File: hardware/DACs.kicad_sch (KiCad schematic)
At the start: 70 parts, among them U10 LTC2642ACDD-16#PBF, U11 LTC2642ACDD-16#PBF, U12 LTC2642ACDD-16#PBF, U13 LT1678CS8#PBF, U14 LT1678CS8#PBF, U15 LT1678CS8#PBF, U16 LT1678CS8#PBF, U17 LT1461CIS8-2.5#PBF, U9 LTC2642ACDD-16#PBF

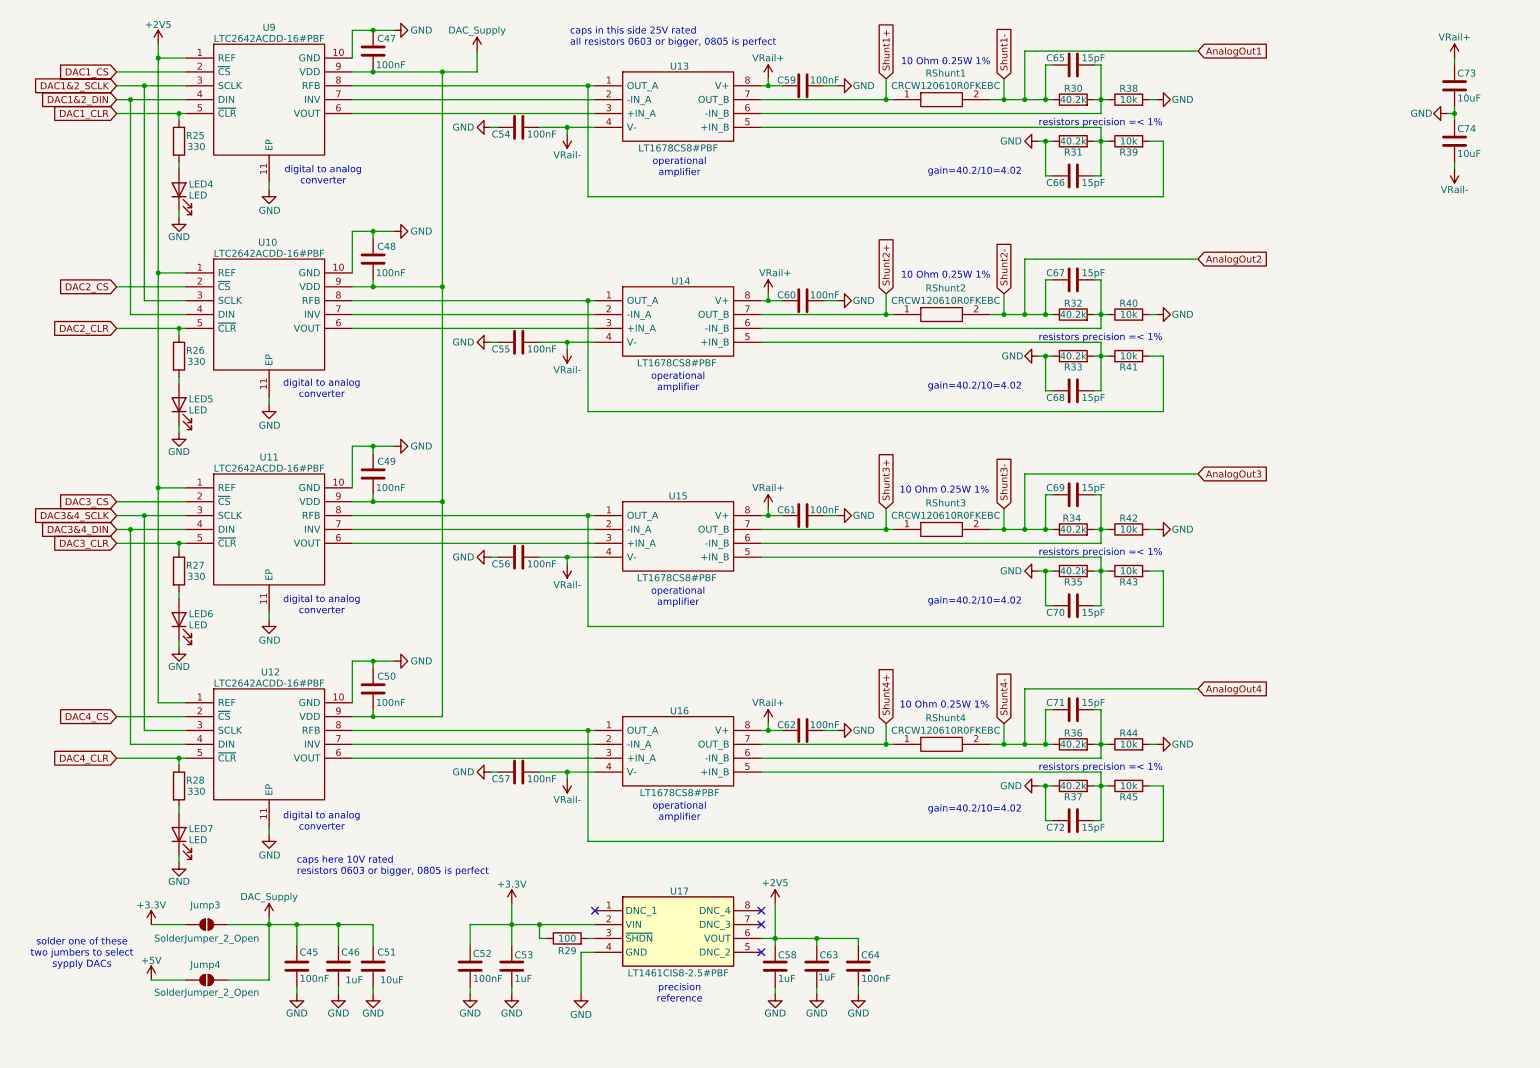
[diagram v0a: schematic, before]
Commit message: Added caps voltage rating + block diagram
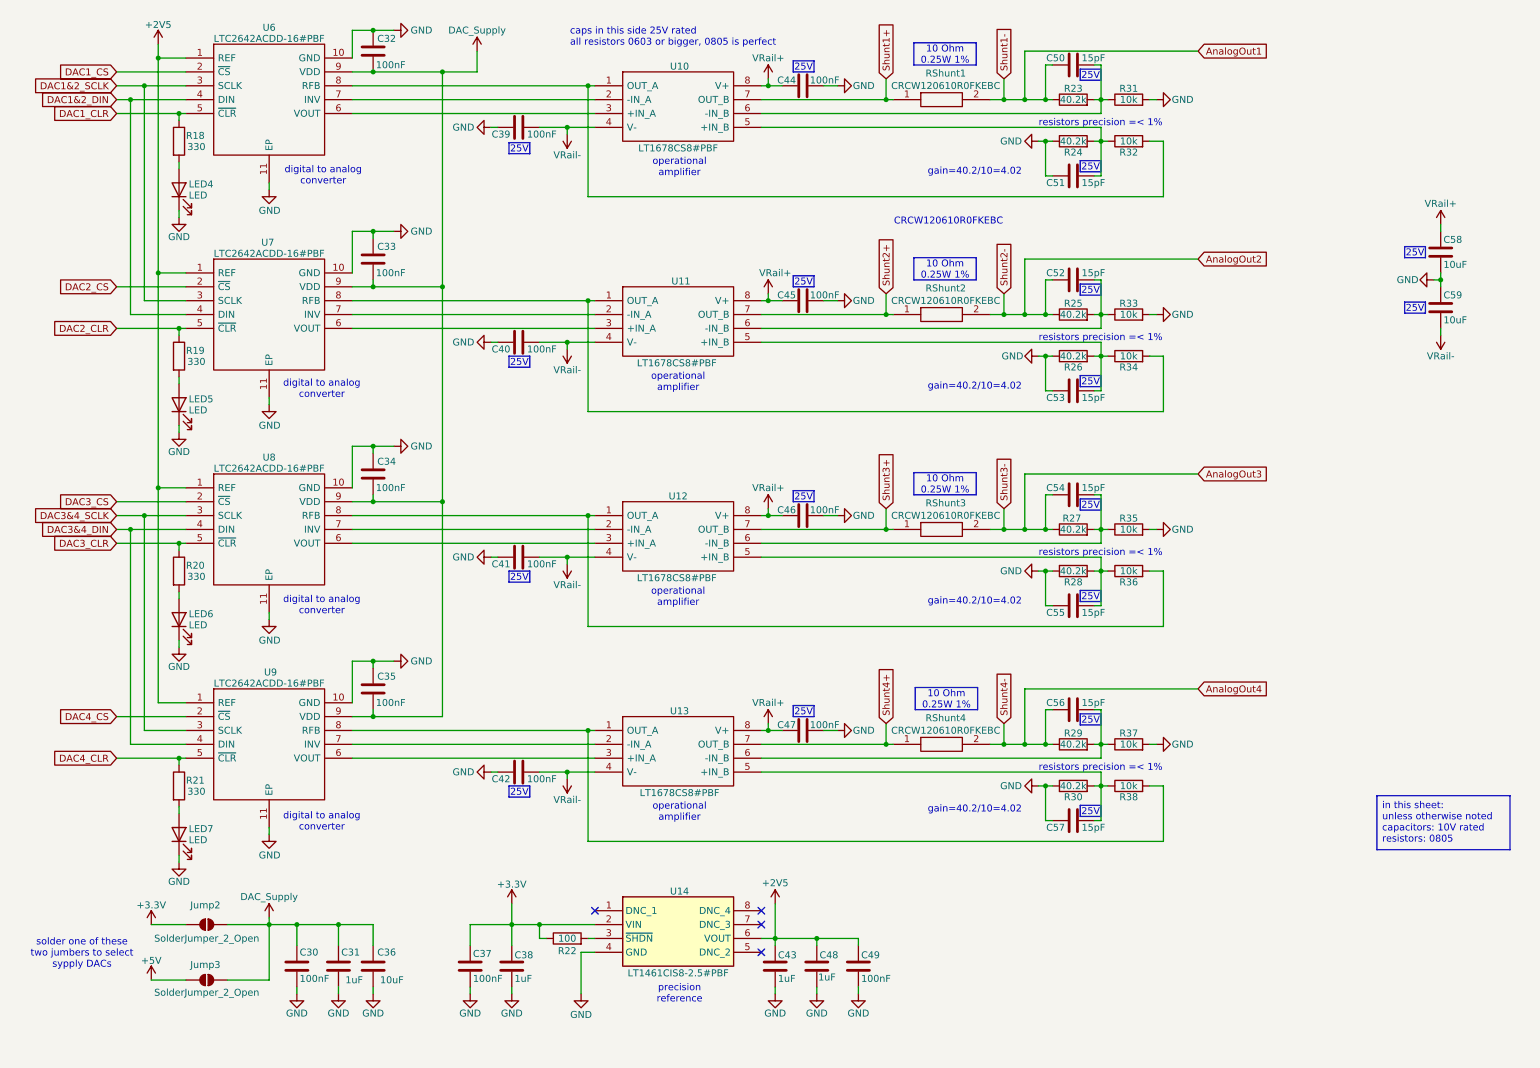
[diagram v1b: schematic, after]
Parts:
- renumbered C45 to C30, C46 to C31, C47 to C32, C48 to C33, C49 to C34, C50 to C35, C51 to C36, C52 to C37, C53 to C38, C54 to C39, C55 to C40, C56 to C41, C57 to C42, C58 to C43, C59 to C44, C60 to C45, C61 to C46, C62 to C47, C63 to C48, C64 to C49, C65 to C50, C66 to C51, C67 to C52, C68 to C53, C69 to C54, C70 to C55, C71 to C56, C72 to C57, C73 to C58, C74 to C59, Jump3 to Jump2, Jump4 to Jump3, R25 to R18, R26 to R19, R27 to R20, R28 to R21, R29 to R22, R30 to R23, R31 to R24, R32 to R25, R33 to R26, R34 to R27, R35 to R28, R36 to R29, R37 to R30, R38 to R31, R39 to R32, R40 to R33, R41 to R34, R42 to R35, R43 to R36, R44 to R37, R45 to R38, U13 to U10, U14 to U11, U15 to U12, U16 to U13, U17 to U14, U9 to U6, U10 to U7, U11 to U8, U12 to U9
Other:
- note added: "CRCW120610R0FKEBC"
- note removed: "10 Ohm 0.25W 1%"
- note removed: "caps here 10V rated resistors 0603 or bigger, 0805 is perfect"
- title: Multi Channel HARP DAC -> harp device quad dac
- moved on the sheet: C58, C59

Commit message: The footprint assigning and reviewing have started.
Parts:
- C30, C31, C32, C33, C34, C35, C36, C37, C38, C39, C40, C41, C42, C43, C44, C45, C46, C47, C48, C49, C50, C51, C52, C53, C54, C55, C56, C57, C58, C59: symbol Device:C -> harp.device.quad.dac:C
- Jump2, Jump3: symbol Jumper:SolderJumper_2_Open -> harp.device.quad.dac:SolderJumper_2_Open
- LED4, LED5, LED6, LED7: symbol Device:LED -> harp.device.quad.dac:LED
- R18, R19, R20, R21, R22, R23, R24, R25, R26, R27, R28, R29, R30, R31, R32, R33, R34, R35, R36, R37, R38: symbol Device:R -> harp.device.quad.dac:R
- RShunt1, RShunt2, RShunt3, RShunt4: symbol CRCW120610R0FKEBC:CRCW120610R0FKEBC -> harp.device.quad.dac:CRCW120610R0FKEBC
- U10, U11, U12, U13: symbol LT1678CS8#PBF:LT1678CS8#PBF -> harp.device.quad.dac:LT1678CS8#PBF
- U14: symbol LT1461CIS8-2_5#PBF:LT1461CIS8-2.5#PBF -> harp.device.quad.dac:LT1461CIS8-2.5#PBF
- U6, U7, U8, U9: symbol LTC2642ACDD-16#PBF:LTC2642ACDD-16#PBF -> harp.device.quad.dac:LTC2642ACDD-16#PBF

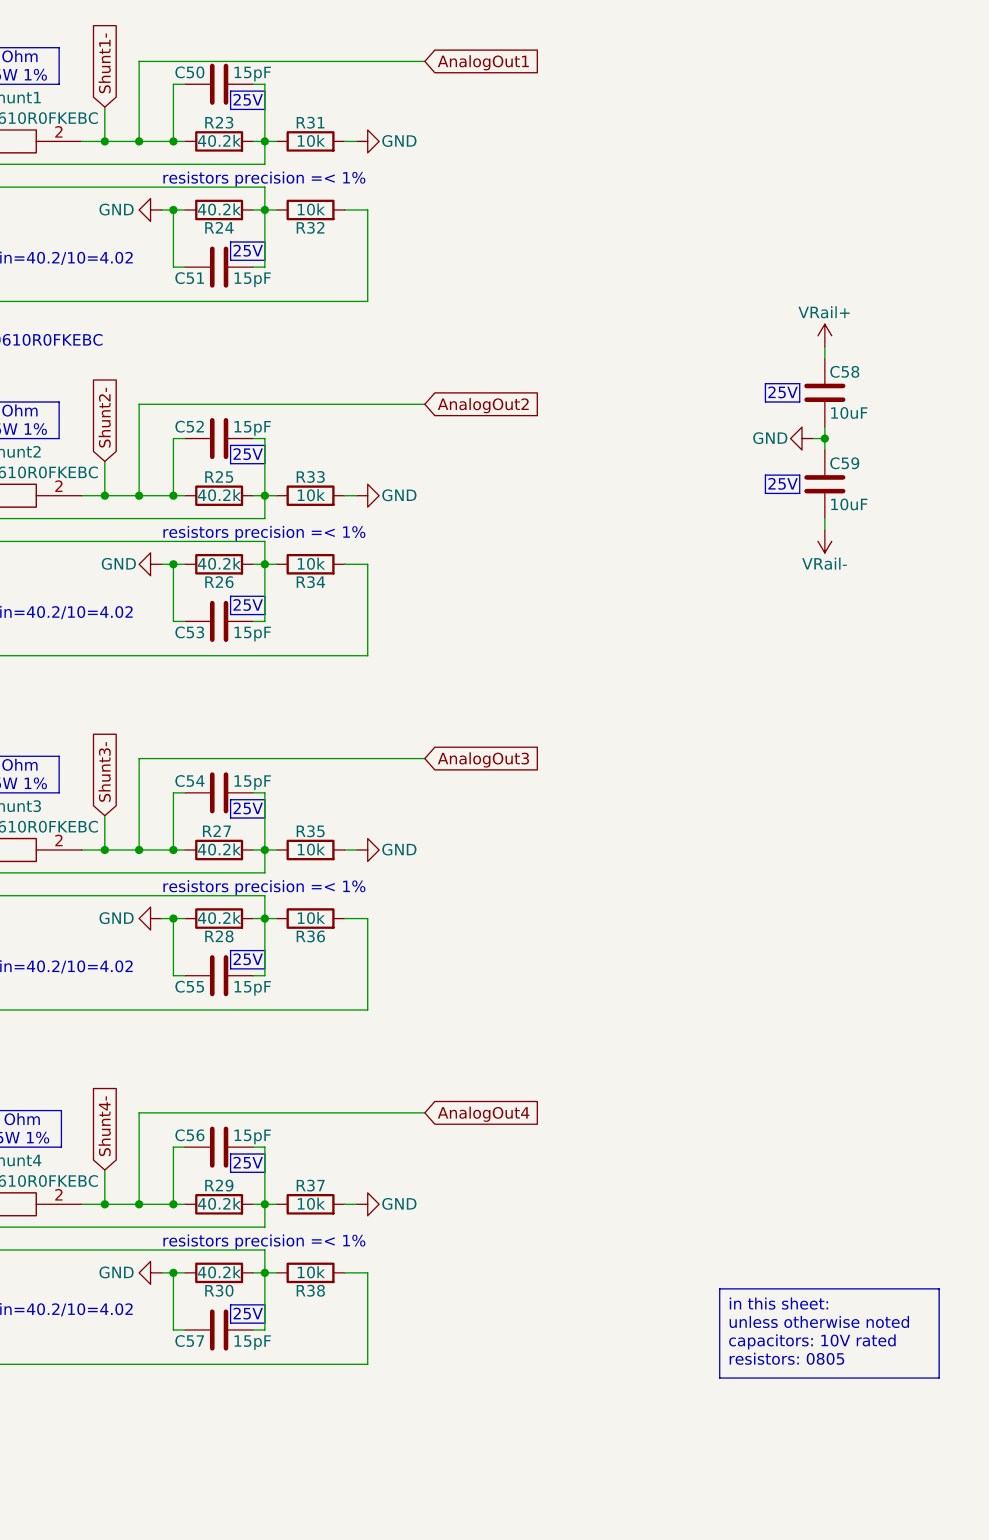
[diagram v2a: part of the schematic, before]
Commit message: Modified notes about caps and resistors
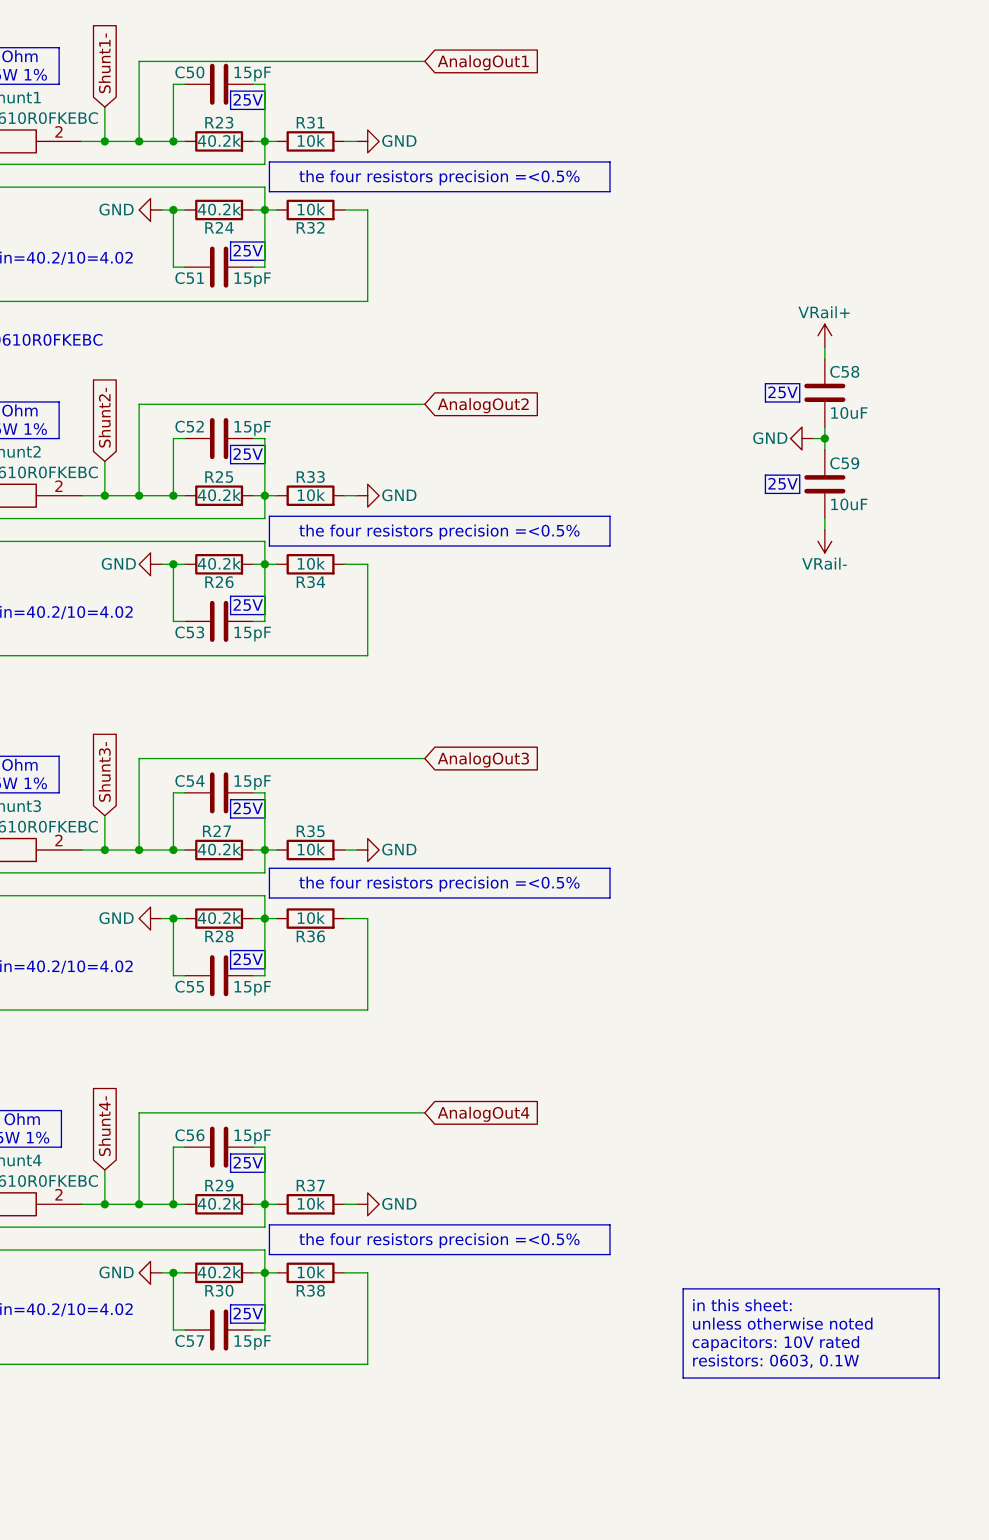
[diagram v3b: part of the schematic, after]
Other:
- note removed: "resistors precision =< 1%"
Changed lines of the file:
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@@
 		)
 	)
-	(text "resistors precision =< 1%"
-		(exclude_from_sim no)
-		(at 198.12 151.13 0)
+	(text "operational\namplifier"
+		(exclude_from_sim no)
+		(at 132.08 120.904 0)
+		(effects
+			(font
+				(size 1.27 1.27)
+			)
+			(justify bottom)
+		)
+	)
+	(text "gain=40.2/10=4.02"
+		(exclude_from_sim no)
+		(at 177.8 81.28 0)
 		(effects
 			(font
@@
 		)
 	)
+	(text "digital to analog\nconverter"
+		(exclude_from_sim no)
+		(at 66.802 162.052 0)
+		(effects
+			(font
+				(size 1.27 1.27)
+			)
+			(justify bottom)
+		)
+	)
+	(text "digital to analog\nconverter"
+		(exclude_from_sim no)
+		(at 66.802 122.428 0)
+		(effects
+			(font
+				(size 1.27 1.27)
+			)
+			(justify bottom)
+		)
+	)
+	(text "CRCW120610R0FKEBC"
+		(exclude_from_sim no)
+		(at 181.61 50.292 0)
+		(effects
+			(font
+				(size 1.27 1.27)
+			)
+		)
+	)
 	(text "operational\namplifier"
 		(exclude_from_sim no)
-		(at 132.08 120.904 0)
+		(at 132.334 160.274 0)
 		(effects
 			(font
@@
 		)
 	)
+	(text "caps in this side 25V rated\nall resistors 0603 or bigger, 0805 is perfect"
+		(exclude_from_sim no)
+		(at 112.268 16.51 0)
+		(effects
+			(font
+				(size 1.27 1.27)
+			)
+			(justify left)
+		)
+	)
 	(text "gain=40.2/10=4.02"
 		(exclude_from_sim no)
-		(at 177.8 81.28 0)
+		(at 177.8 158.75 0)
 		(effects
 			(font
@@
 	(text "digital to analog\nconverter"
 		(exclude_from_sim no)
-		(at 66.802 162.052 0)
+		(at 67.056 43.688 0)
 		(effects
 			(font
@@
 		)
 	)
-	(text "digital to analog\nconverter"
-		(exclude_from_sim no)
-		(at 66.802 122.428 0)
-		(effects
-			(font
-				(size 1.27 1.27)
-			)
-			(justify bottom)
-		)
-	)
-	(text "CRCW120610R0FKEBC"
-		(exclude_from_sim no)
-		(at 181.61 50.292 0)
-		(effects
-			(font
-				(size 1.27 1.27)
-			)
-		)
-	)
-	(text "resistors precision =< 1%"
-		(exclude_from_sim no)
-		(at 198.12 72.39 0)
+	(text "gain=40.2/10=4.02"
+		(exclude_from_sim no)
+		(at 177.8 120.65 0)
 		(effects
 			(font
@@
 		)
 	)
-	(text "operational\namplifier"
-		(exclude_from_sim no)
-		(at 132.334 160.274 0)
-		(effects
-			(font
-				(size 1.27 1.27)
-			)
-			(justify bottom)
-		)
-	)
-	(text "caps in this side 25V rated\nall resistors 0603 or bigger, 0805 is perfect"
-		(exclude_from_sim no)
-		(at 112.268 16.51 0)
-		(effects
-			(font
-				(size 1.27 1.27)
-			)
-			(justify left)
-		)
-	)
-	(text "gain=40.2/10=4.02"
-		(exclude_from_sim no)
-		(at 177.8 158.75 0)
-		(effects
-			(font
-				(size 1.27 1.27)
-			)
-			(justify left bottom)
-		)
-	)
-	(text "resistors precision =< 1%"
-		(exclude_from_sim no)
-		(at 198.12 33.02 0)
-		(effects
-			(font
-				(size 1.27 1.27)
-			)
-			(justify left bottom)
-		)
-	)
-	(text "digital to analog\nconverter"
-		(exclude_from_sim no)
-		(at 67.056 43.688 0)
-		(effects
-			(font
-				(size 1.27 1.27)
-			)
-			(justify bottom)
-		)
-	)
-	(text "gain=40.2/10=4.02"
-		(exclude_from_sim no)
-		(at 177.8 120.65 0)
-		(effects
-			(font
-				(size 1.27 1.27)
-			)
-			(justify left bottom)
-		)
-	)
 	(text "solder one of these\ntwo jumbers to select\nsypply DACs"
 		(exclude_from_sim no)
@@
 				(size 1.27 1.27)
 			)
-		)
-	)
-	(text "resistors precision =< 1%"
-		(exclude_from_sim no)
-		(at 198.12 111.76 0)
-		(effects
-			(font
-				(size 1.27 1.27)
-			)
-			(justify left bottom)
 		)
 	)
@@
 		)
 	)
-	(text_box "in this sheet:\nunless otherwise noted\ncapacitors: 10V rated \nresistors: 0805"
-		(exclude_from_sim no)
-		(at 260.096 155.448 0)
-		(size 24.384 9.906)
-		(margins 0.9525 0.9525 0.9525 0.9525)
-		(stroke
-			(width 0)
-			(type solid)
-		)
-		(fill
-			(type color)
-			(color 0 255 0 1)
-		)
-		(effects
-			(font
-				(size 1.27 1.27)
-			)
-			(justify left top)
+	(text_box "in this sheet:\nunless otherwise noted\ncapacitors: 10V rated \nresistors: 0603, 0.1W"
+		(exclude_from_sim no)
+		(at 256.032 155.448 0)
+		(size 28.448 9.906)
+		(margins 0.9525 0.9525 0.9525 0.9525)
+		(stroke
+			(width 0)
+			(type solid)
+		)
+		(fill
+			(type color)
+			(color 0 255 0 1)
+		)
+		(effects
+			(font
+				(size 1.27 1.27)
+			)
+			(justify left)
 		)
 	)
@@
 		)
 	)
+	(text_box "the four resistors precision =<0.5%"
+		(exclude_from_sim no)
+		(at 210.058 148.336 0)
+		(size 37.846 3.302)
+		(margins 0.9525 0.9525 0.9525 0.9525)
+		(stroke
+			(width 0)
+			(type solid)
+		)
+		(fill
+			(type color)
+			(color 0 255 0 1)
+		)
+		(effects
+			(font
+				(size 1.27 1.27)
+			)
+		)
+	)
 	(text_box "25V"
 		(exclude_from_sim no)
@@
 		)
 	)
+	(text_box "the four resistors precision =<0.5%"
+		(exclude_from_sim no)
+		(at 210.058 30.226 0)
+		(size 37.846 3.302)
+		(margins 0.9525 0.9525 0.9525 0.9525)
+		(stroke
+			(width 0)
+			(type solid)
+		)
+		(fill
+			(type color)
+			(color 0 255 0 1)
+		)
+		(effects
+			(font
+				(size 1.27 1.27)
+			)
+		)
+	)
 	(text_box "25V"
 		(exclude_from_sim no)
 		(at 101.092 35.814 0)
 		(size 3.81 2.032)
+		(margins 0.9525 0.9525 0.9525 0.9525)
+		(stroke
+			(width 0)
+			(type solid)
+		)
+		(fill
+			(type color)
+			(color 0 255 0 1)
+		)
+		(effects
+			(font
+				(size 1.27 1.27)
+			)
+		)
+	)
+	(text_box "the four resistors precision =<0.5%"
+		(exclude_from_sim no)
+		(at 210.058 108.712 0)
+		(size 37.846 3.302)
 		(margins 0.9525 0.9525 0.9525 0.9525)
 		(stroke
@@
 		(margins 0.9525 0.9525 0.9525 0.9525)
 		(stroke
+			(width 0)
+			(type solid)
+		)
+		(fill
+			(type color)
+			(color 0 255 0 1)
+		)
+		(effects
+			(font
+				(size 1.27 1.27)
+			)
+		)
+	)
+	(text_box "the four resistors precision =<0.5%"
+		(exclude_from_sim no)
+		(at 210.058 69.596 0)
+		(size 37.846 3.302)
+		(margins 0.9525 0.9525 0.9525 0.9525)
+		(stroke

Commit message: Updating some footprints
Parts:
- C30, C31, C32, C33, C34, C35, C37, C38, C39, C40, C41, C42, C43, C44, C45, C46, C47, C48, C49, C50, C51, C52, C53, C54, C55, C56, C57: footprint Capacitor_SMD:C_0402_1005Metric -> Capacitor_SMD:C_0603_1608Metric; symbol harp.device.quad.dac:C -> harp.device.quad.dac:C_0603
- C36, C58, C59: footprint Capacitor_SMD:C_0805_2012Metric -> Capacitor_SMD:C_0603_1608Metric; symbol harp.device.quad.dac:C -> harp.device.quad.dac:C_0603
- Jump2, Jump3: footprint (none) -> harp.device.quad.dac.kicad:R_0603_1608Metric_Pad0.98x0.95mm_HandSolder
- LED4, LED5, LED6, LED7: footprint LED_SMD:LED_0603_1608Metric_Pad1.05x0.95mm_HandSolder -> harp.device.quad.dac.kicad:LED_0603_1608Metric_Pad1.05x0.95mm_HandSolder; MFN (none) -> SunLED; MPN (none) -> XZCDGK53W-1VF
- R18, R19, R20, R21, R22, R23, R24, R25, R26, R27, R28, R29, R30, R31, R32, R33, R34, R35, R36, R37, R38: footprint Resistor_SMD:R_0402_1005Metric -> Resistor_SMD:R_0603_1608Metric; symbol harp.device.quad.dac:R -> harp.device.quad.dac:R_0603
- RShunt1, RShunt2, RShunt3, RShunt4: footprint RESC3216X60N -> Resistor_SMD:R_1206_3216Metric
- U10, U11, U12, U13, U14: footprint SOIC127P599X175-8N -> harp.device.quad.dac.kicad:SOIC127P599X175-8N
- U6, U7, U8, U9: footprint SON50P300X300X80-11N-D -> harp.device.quad.dac.kicad:SON50P300X300X80-11N-D

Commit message: The layout design has begun.
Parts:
- added J20, J21: Conn_01x02, Connector_PinHeader_2.54mm:PinHeader_1x02_P2.54mm_Vertical, symbol harp.device.quad.dac:Conn_01x02
- Jump3: now not fitted; now left out of the parts list
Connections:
- net +3.3V: now also J20.1 (Pin_1)
- net +5V: now also J21.2 (Pin_2)
- net DAC_Supply: now also J20.2 (Pin_2), J21.1 (Pin_1)
